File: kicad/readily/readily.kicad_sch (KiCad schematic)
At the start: 29 parts, among them J1 Conn_01x09_Socket, J2 Micro_SD_Card_Det1, J3 USB_C_Receptacle_USB2.0_16P, J4 Conn_01x03, SW2 SW_SPST, SW3 SW_SPST, U1 ESP32-S3-WROOM-1, U2 BQ24040DSQR, U3 TPD2EUSB30, U4 TLV75533PDRV

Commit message: feat: adding the first stage of the PCB
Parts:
- removed J2: Micro_SD_Card_Det1, symbol Connector:Micro_SD_Card_Det1
- removed R1, R2, R3: 10kΩ, symbol Device:R
- added MICRO_SD1: TF-01A, TF-01A:TF-01A, symbol TF-01A:TF-01A
- added R11, R13, R14: 10kΩ, PCM_JLCPCB:R_0603, symbol Device:R
- C1: footprint (none) -> PCM_JLCPCB:C_0603
- C2, C3: footprint (none) -> PCM_JLCPCB:C_0805
- C4: footprint Capacitor_SMD:C_0402_1005Metric -> PCM_JLCPCB:C_0603
- C5: value 10u -> 10uF; footprint Capacitor_SMD:C_0805_2012Metric -> PCM_JLCPCB:C_0805
- J1: footprint (none) -> Pin01x09:Pins01x09
- J3: footprint (none) -> Connector_USB:USB_C_Receptacle_HRO_TYPE-C-31-M-12
- J4: footprint (none) -> JST_PH_B3B-PH-K_1x03_P2.00mm_Vertical
- R10, R12, R9: footprint Resistor_SMD:R_0402_1005Metric -> PCM_JLCPCB:R_0603
- R4, R5, R6, R7, R8: footprint (none) -> PCM_JLCPCB:R_0603
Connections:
- net +3V3: now also MICRO_SD1.4 (VDD)
- net GND: now also MICRO_SD1.6 (VSS), MICRO_SD1.CD1 (CD), MICRO_SD1.MP1 (SHIELD), MICRO_SD1.MP2 (SHIELD), MICRO_SD1.MP3 (SHIELD), MICRO_SD1.MP4 (SHIELD)
- net SD_CLK: now also MICRO_SD1.5 (CLK)
- net SD_CS: now also R11.1
- net SD_MISO: now also R13.1
- net SD_MOSI: now also R14.1
- new net: MICRO_SD1.7 (DAT0), R13.2
- new net: MICRO_SD1.2 (CD/DAT3), R11.2
- new net: MICRO_SD1.3 (CMD), R14.2

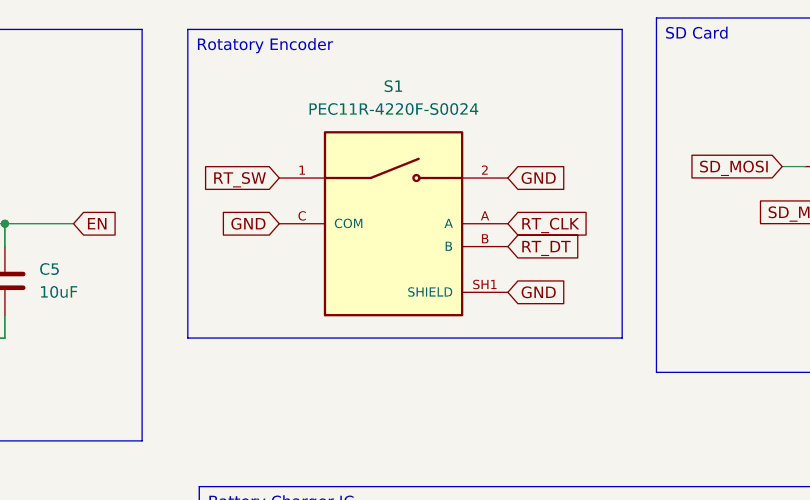
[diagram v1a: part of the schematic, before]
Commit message: feat: updating the specs with the final rotatory encoder switch
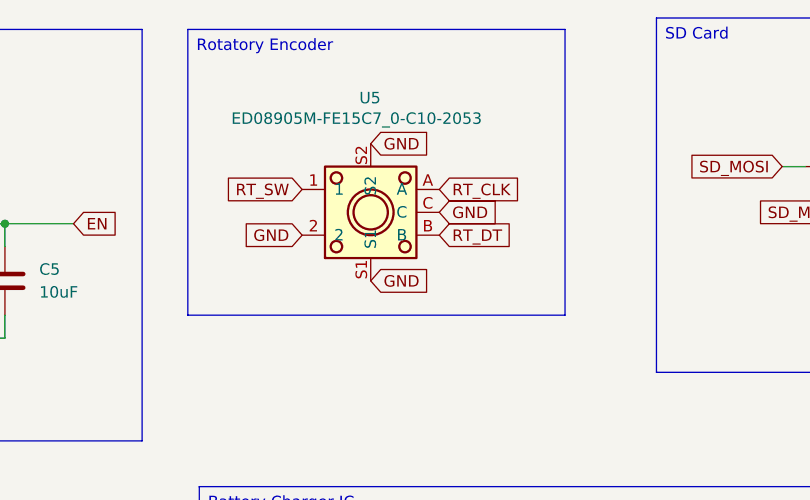
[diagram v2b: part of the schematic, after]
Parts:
- removed S1: PEC11R-4220F-S0024, RotatoryEncoder:XDCR_PEC11R-4220F-S0024, symbol RotatoryEncoder:PEC11R-4220F-S0024
- added U5: ED08905M-FE15C7_0-C10-2053, JLCPCB Import:ED08905M-FE15C7_0-C10-2053, symbol ED08905M-FE15C7.0-C10-2053:ED08905M-FE15C7_0-C10-2053
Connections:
- net GND: now also U5.2, U5.C, U5.S1, U5.S2
- net RT_CLK: now also U5.A
- net RT_DT: now also U5.B
- net RT_SW: now also U5.1

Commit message: feat: version 1.0 of the pcb
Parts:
- removed J4: Conn_01x03, JST_PH_B3B-PH-K_1x03_P2.00mm_Vertical, symbol Connector_Generic:Conn_01x03
- added U6: WAFER-PH2_0-3PWB, JLCImport:WAFER-PH2_0-3PWB, symbol ED08905M-FE15C7.0-C10-2053:WAFER-PH2_0-3PWB
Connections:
- net BAT_NTC: now also U6.2
- net GND: now also U6.3, U6.4, U6.5
- net SYS_OUT: now also U6.1

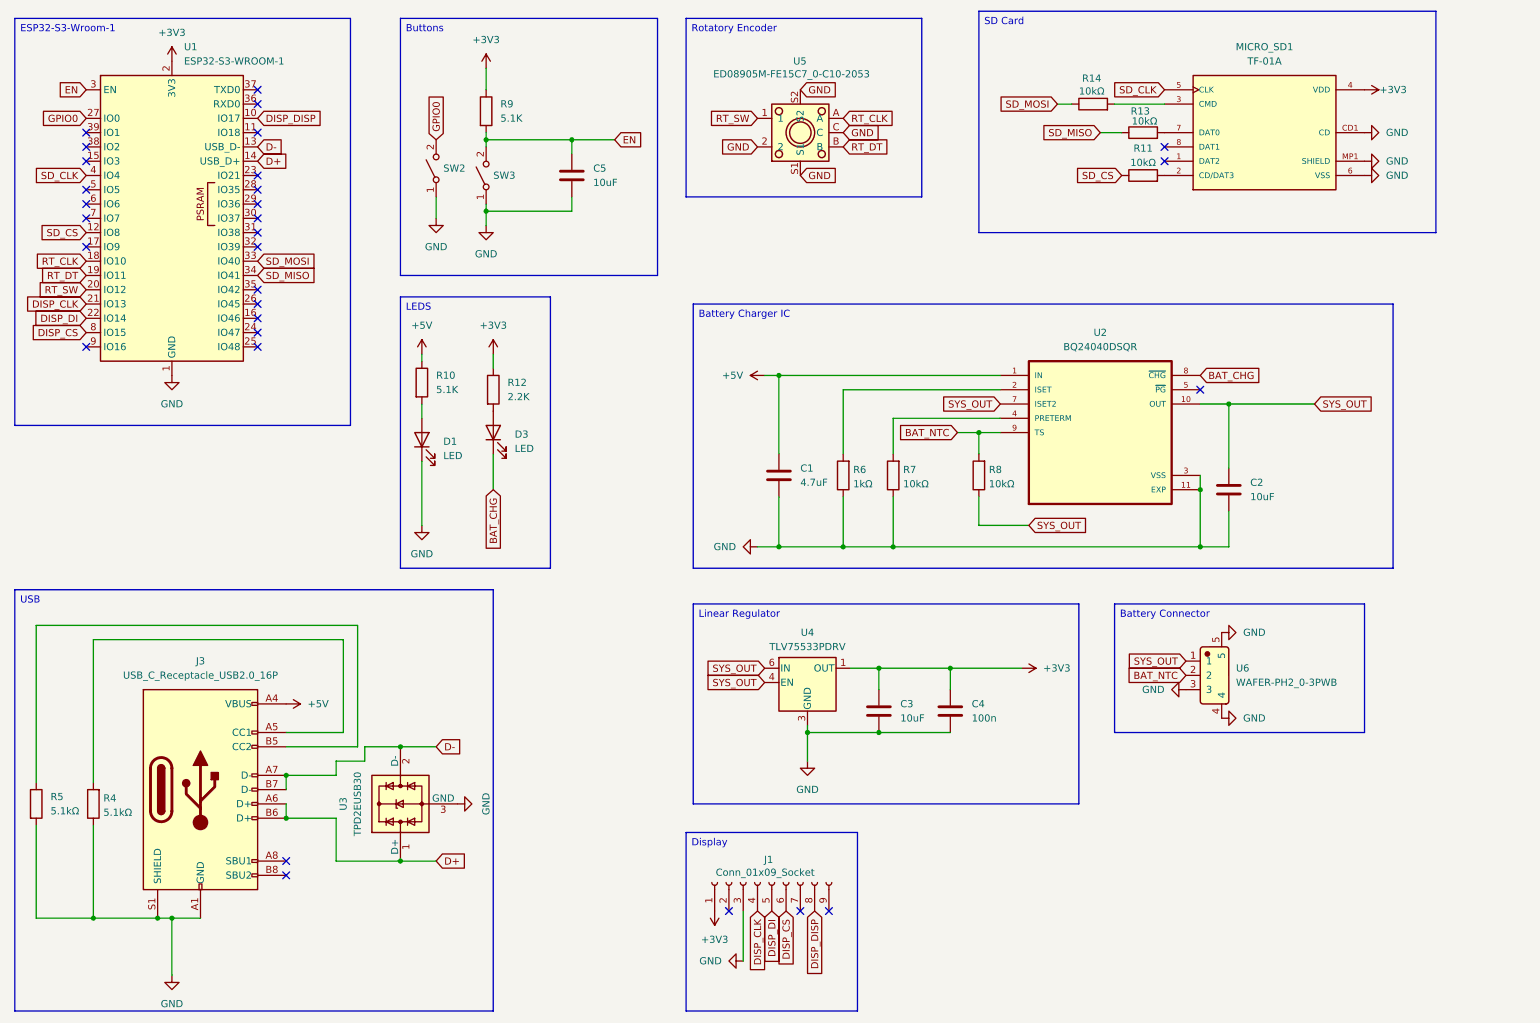
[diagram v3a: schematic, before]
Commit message: feat: adding logo to pcb, improving component placement and changing the battery connector to two pin JST
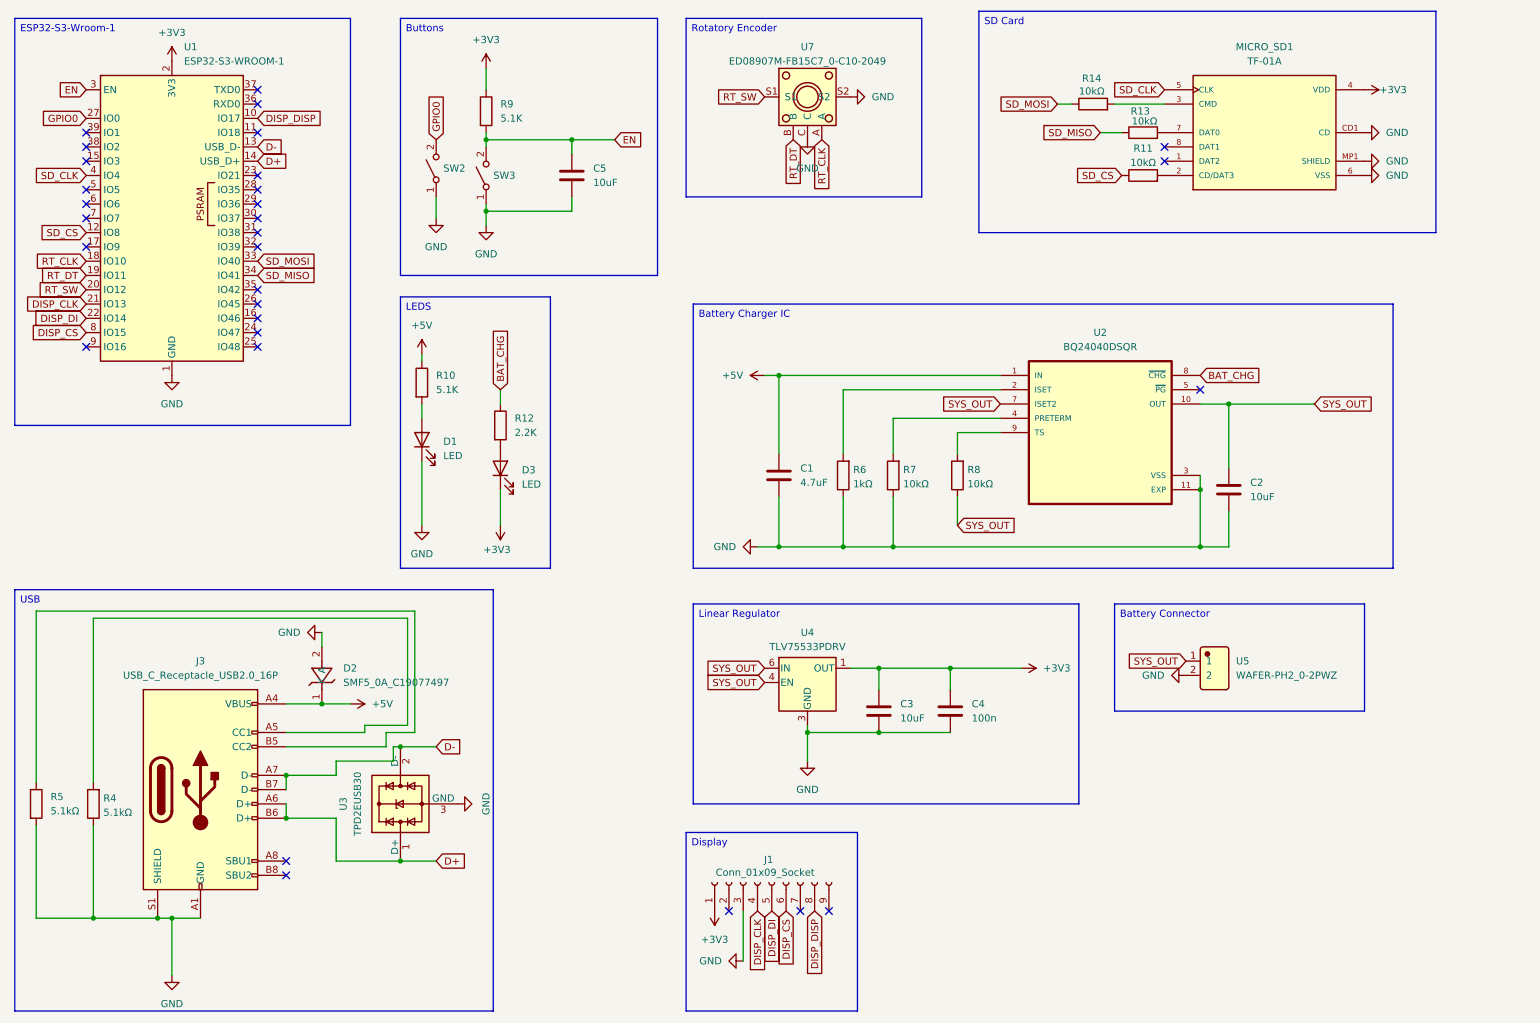
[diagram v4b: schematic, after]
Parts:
- removed U5: ED08905M-FE15C7_0-C10-2053, JLCPCB Import:ED08905M-FE15C7_0-C10-2053, symbol ED08905M-FE15C7.0-C10-2053:ED08905M-FE15C7_0-C10-2053
- removed U6: WAFER-PH2_0-3PWB, JLCImport:WAFER-PH2_0-3PWB, symbol ED08905M-FE15C7.0-C10-2053:WAFER-PH2_0-3PWB
- added D2: SMF5_0A_C19077497, JLCImport:SMF5_0A_C19077497, symbol JLCImport:SMF5_0A_C19077497
- added U5: WAFER-PH2_0-2PWZ, JLCImport:WAFER-PH2_0-2PWZ, symbol JLCImport:WAFER-PH2_0-2PWZ
- added U7: ED08907M-FB15C7_0-C10-2049, JLCImport:ED08907M-FB15C7_0-C10-2049, symbol JLCImport:ED08907M-FB15C7_0-C10-2049
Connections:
- net +3V3: now also D3.1 (K); no longer R12.1
- net +5V: now also D2.1 (K)
- net BAT_CHG: now also R12.1; no longer D3.1 (K)
- net GND: now also D2.2 (A), U5.2, U7.C, U7.S2
- net RT_CLK: now also U7.A
- net RT_DT: now also U7.B
- net RT_SW: now also U7.S1
- net SYS_OUT: now also U5.1
- net BAT_NTC: no longer names the net of R8.2, U2.9 (TS)
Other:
- title: Readily -> Motif
- moved on the sheet: D3, R12, R8

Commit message: feat: finishing the power refactor on the board
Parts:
- added C6: 47uF, PCM_JLCPCB:C_0805, symbol Device:C
- added C7, C8: 100nF, PCM_JLCPCB:C_0805, symbol Device:C
- added C9: 10uF, PCM_JLCPCB:C_0805, symbol Device:C
- added R1: 10K, PCM_JLCPCB:R_0603, symbol Device:R
- C2: value 10uF -> 22uF
- R7: value 10kΩ -> 2kΩ
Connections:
- net +3V3: now also R11.2, R13.2, R14.2, C6.2, C7.2, C8.1, C9.1, R1.1
- net GND: now also C6.1, C7.1, C8.2, C9.2
- net GPIO0: now also R1.2
- net SD_CS: now also MICRO_SD1.2 (CD/DAT3)
- net SD_MISO: now also MICRO_SD1.7 (DAT0)
- net SD_MOSI: now also MICRO_SD1.3 (CMD)
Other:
- moved on the sheet: C5, D1, D3, MICRO_SD1, R10, R11, R12, R13, R14, R9, SW2, SW3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

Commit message: feat: updating and rerouting all components
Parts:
- C1, C4: footprint PCM_JLCPCB:C_0603 -> Capacitor_SMD:C_0603_1608Metric
- C2, C3, C5, C6, C7, C8, C9: footprint PCM_JLCPCB:C_0805 -> Capacitor_SMD:C_0805_2012Metric
- J1: footprint Pin01x09:Pins01x09 -> Pins01x09:Pins01x09
- MICRO_SD1: footprint TF-01A:TF-01A -> SD_Card:TF-01A
- R1, R10, R11, R12, R13, R14, R4, R5, R6, R7, R8, R9: footprint PCM_JLCPCB:R_0603 -> Resistor_SMD:R_0603_1608Metric
- U2: footprint BQ24040DSQR:SON40P200X200X80-11N -> Package_DFN_QFN:Texas_DSQ0010A_WSON-10-1EP_2x2mm_P0.4mm_EP0.9x1.5mm
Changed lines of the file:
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@@
 			)
 		)
-		(property "Footprint" "PCM_JLCPCB:C_0805"
+		(property "Footprint" "Capacitor_SMD:C_0805_2012Metric"
 			(at 266.7 35.2552 0)
 			(effects
@@
 			)
 		)
-		(property "Footprint" "PCM_JLCPCB:R_0603"
+		(property "Footprint" "Resistor_SMD:R_0603_1608Metric"
 			(at 184.658 96.52 90)
 			(effects
@@
 			)
 		)
-		(property "Footprint" "PCM_JLCPCB:R_0603"
+		(property "Footprint" "Resistor_SMD:R_0603_1608Metric"
 			(at 211.328 33.02 90)
 			(effects
@@
 			)
 		)
-		(property "Footprint" "PCM_JLCPCB:R_0603"
+		(property "Footprint" "Resistor_SMD:R_0603_1608Metric"
 			(at 17.272 154.94 90)
 			(effects
@@
 			)
 		)
-		(property "Footprint" "PCM_JLCPCB:C_0805"
+		(property "Footprint" "Capacitor_SMD:C_0805_2012Metric"
 			(at 266.7 22.5552 0)
 			(effects
@@
 			)
 		)
-		(property "Footprint" "PCM_JLCPCB:C_0805"
+		(property "Footprint" "Capacitor_SMD:C_0805_2012Metric"
 			(at 64.77 34.5948 0)
 			(effects
@@
 			)
 		)
-		(property "Footprint" "PCM_JLCPCB:R_0603"
+		(property "Footprint" "Resistor_SMD:R_0603_1608Metric"
 			(at 218.948 33.02 90)
 			(effects
@@
 			)
 		)
-		(property "Footprint" "PCM_JLCPCB:R_0603"
+		(property "Footprint" "Resistor_SMD:R_0603_1608Metric"
 			(at 89.662 80.01 90)
 			(effects
@@
 			)
 		)
-		(property "Footprint" "PCM_JLCPCB:R_0603"
+		(property "Footprint" "Resistor_SMD:R_0603_1608Metric"
 			(at 30.988 154.94 90)
 			(effects
@@
 			)
 		)
-		(property "Footprint" "PCM_JLCPCB:R_0603"
+		(property "Footprint" "Resistor_SMD:R_0603_1608Metric"
 			(at 112.522 33.02 90)
 			(effects
@@
 			)
 		)
-		(property "Footprint" "PCM_JLCPCB:C_0805"
+		(property "Footprint" "Capacitor_SMD:C_0805_2012Metric"
 			(at 232.1052 102.87 0)
 			(effects
@@
 			)
 		)
-		(property "Footprint" "Pin01x09:Pins01x09"
+		(property "Footprint" "Pins01x09:Pins01x09"
 			(at 149.86 168.91 0)
 			(effects
@@
 			)
 		)
-		(property "Footprint" "PCM_JLCPCB:C_0805"
+		(property "Footprint" "Capacitor_SMD:C_0805_2012Metric"
 			(at 169.8752 142.24 0)
 			(effects
@@
 			)
 		)
-		(property "Footprint" "PCM_JLCPCB:R_0603"
+		(property "Footprint" "Resistor_SMD:R_0603_1608Metric"
 			(at 204.978 33.02 90)
 			(effects
@@
 			)
 		)
-		(property "Footprint" "PCM_JLCPCB:R_0603"
+		(property "Footprint" "Resistor_SMD:R_0603_1608Metric"
 			(at 103.632 87.63 90)
 			(effects
@@
 			)
 		)
-		(property "Footprint" "PCM_JLCPCB:C_0603"
+		(property "Footprint" "Capacitor_SMD:C_0603_1608Metric"
 			(at 152.0952 100.33 0)
 			(effects
@@
 			)
 		)
-		(property "Footprint" "PCM_JLCPCB:R_0603"
+		(property "Footprint" "Resistor_SMD:R_0603_1608Metric"
 			(at 164.338 96.52 90)
 			(effects
@@
 			)
 		)
-		(property "Footprint" "PCM_JLCPCB:R_0603"
+		(property "Footprint" "Resistor_SMD:R_0603_1608Metric"
 			(at 99.822 27.94 90)
 			(effects
@@
 			)
 		)
-		(property "Footprint" "BQ24040DSQR:SON40P200X200X80-11N"
+		(property "Footprint" "Package_DFN_QFN:Texas_DSQ0010A_WSON-10-1EP_2x2mm_P0.4mm_EP0.9x1.5mm"
 			(at 208.28 88.9 0)
 			(effects
@@
 			)
 		)
-		(property "Footprint" "PCM_JLCPCB:C_0603"
+		(property "Footprint" "Capacitor_SMD:C_0603_1608Metric"
 			(at 182.5752 142.24 0)
 			(effects
@@
 			)
 		)
-		(property "Footprint" "PCM_JLCPCB:R_0603"
+		(property "Footprint" "Resistor_SMD:R_0603_1608Metric"
 			(at 173.228 96.52 90)
 			(effects
@@
 			)
 		)
-		(property "Footprint" "TF-01A:TF-01A"
+		(property "Footprint" "SD_Card:TF-01A"
 			(at 238.76 52.07 0)
 			(effects
@@
 			)
 		)
-		(property "Footprint" "PCM_JLCPCB:C_0805"
+		(property "Footprint" "Capacitor_SMD:C_0805_2012Metric"
 			(at 64.77 29.5148 0)
 			(effects
@@
 			)
 		)
-		(property "Footprint" "PCM_JLCPCB:C_0805"
+		(property "Footprint" "Capacitor_SMD:C_0805_2012Metric"
 			(at 130.5052 48.26 0)
 			(effects
